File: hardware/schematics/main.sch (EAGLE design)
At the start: 332 parts, among them IC1 74LS257N, IC10 74S181N, IC100 74S257N, IC101 74LS377N, IC102 74LS377N, IC103 74S153N, IC104 74LS257N, IC105 74LS148N, IC106 74LS377N, IC107 74LS74N, IC108 74LS74N, IC109 74LS377N, IC11 74S181N, IC110 74LS377N, IC111 74LS253N, IC112 74LS257N, IC113 74LS253N, IC114 74LS257N, IC115 74LS04N, IC116 74S153N, IC117 74LS377N, IC118 74LS257N, IC119 74S08N, IC12 74LS151N, IC120 74LS244N, IC121 74LS257N, IC122 74LS257N, IC123 74LS377N, IC124 74S153N, IC125 74LS257N, IC126 74LS74N, IC127 74LS257N, IC128 74157N, IC129 74157N, IC13 74LS257N, IC130 74LS151N, IC131 74157N, IC132 74157N, IC133 74LS151N, IC134 74273N, IC135 74273N, IC136 74273N, IC137 74LS74N, IC138 74LS04N, IC139 74LS00N, IC14 74LS151N, IC141 74LS151N, IC142 74LS257N, IC143 74LS08N, IC144 74LS151N, IC145 7410N, IC146 74LS08N, IC147 74LS257N, IC148 74LS00N, IC149 74LS138N, IC15 74LS257N, IC150 74HC244N, IC151 7432N, IC152 74LS151N, IC153 7432N, IC154 74LS04N, IC155 74LS04N, IC156 74LS04N, IC157 74LS377N, IC158 74LS377N, IC159 74LS377N, IC16 74LS151N, IC160 74LS151N, IC161 74LS244N, IC162 74LS377N, IC163 74LS244N, IC164 74LS138N, IC165 74LS377N, IC166 74LS377N, IC167 7432N, IC168 74LS20N, IC169 74LS377N, IC17 74HC244N, IC170 74LS253N, IC171 74LS377N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

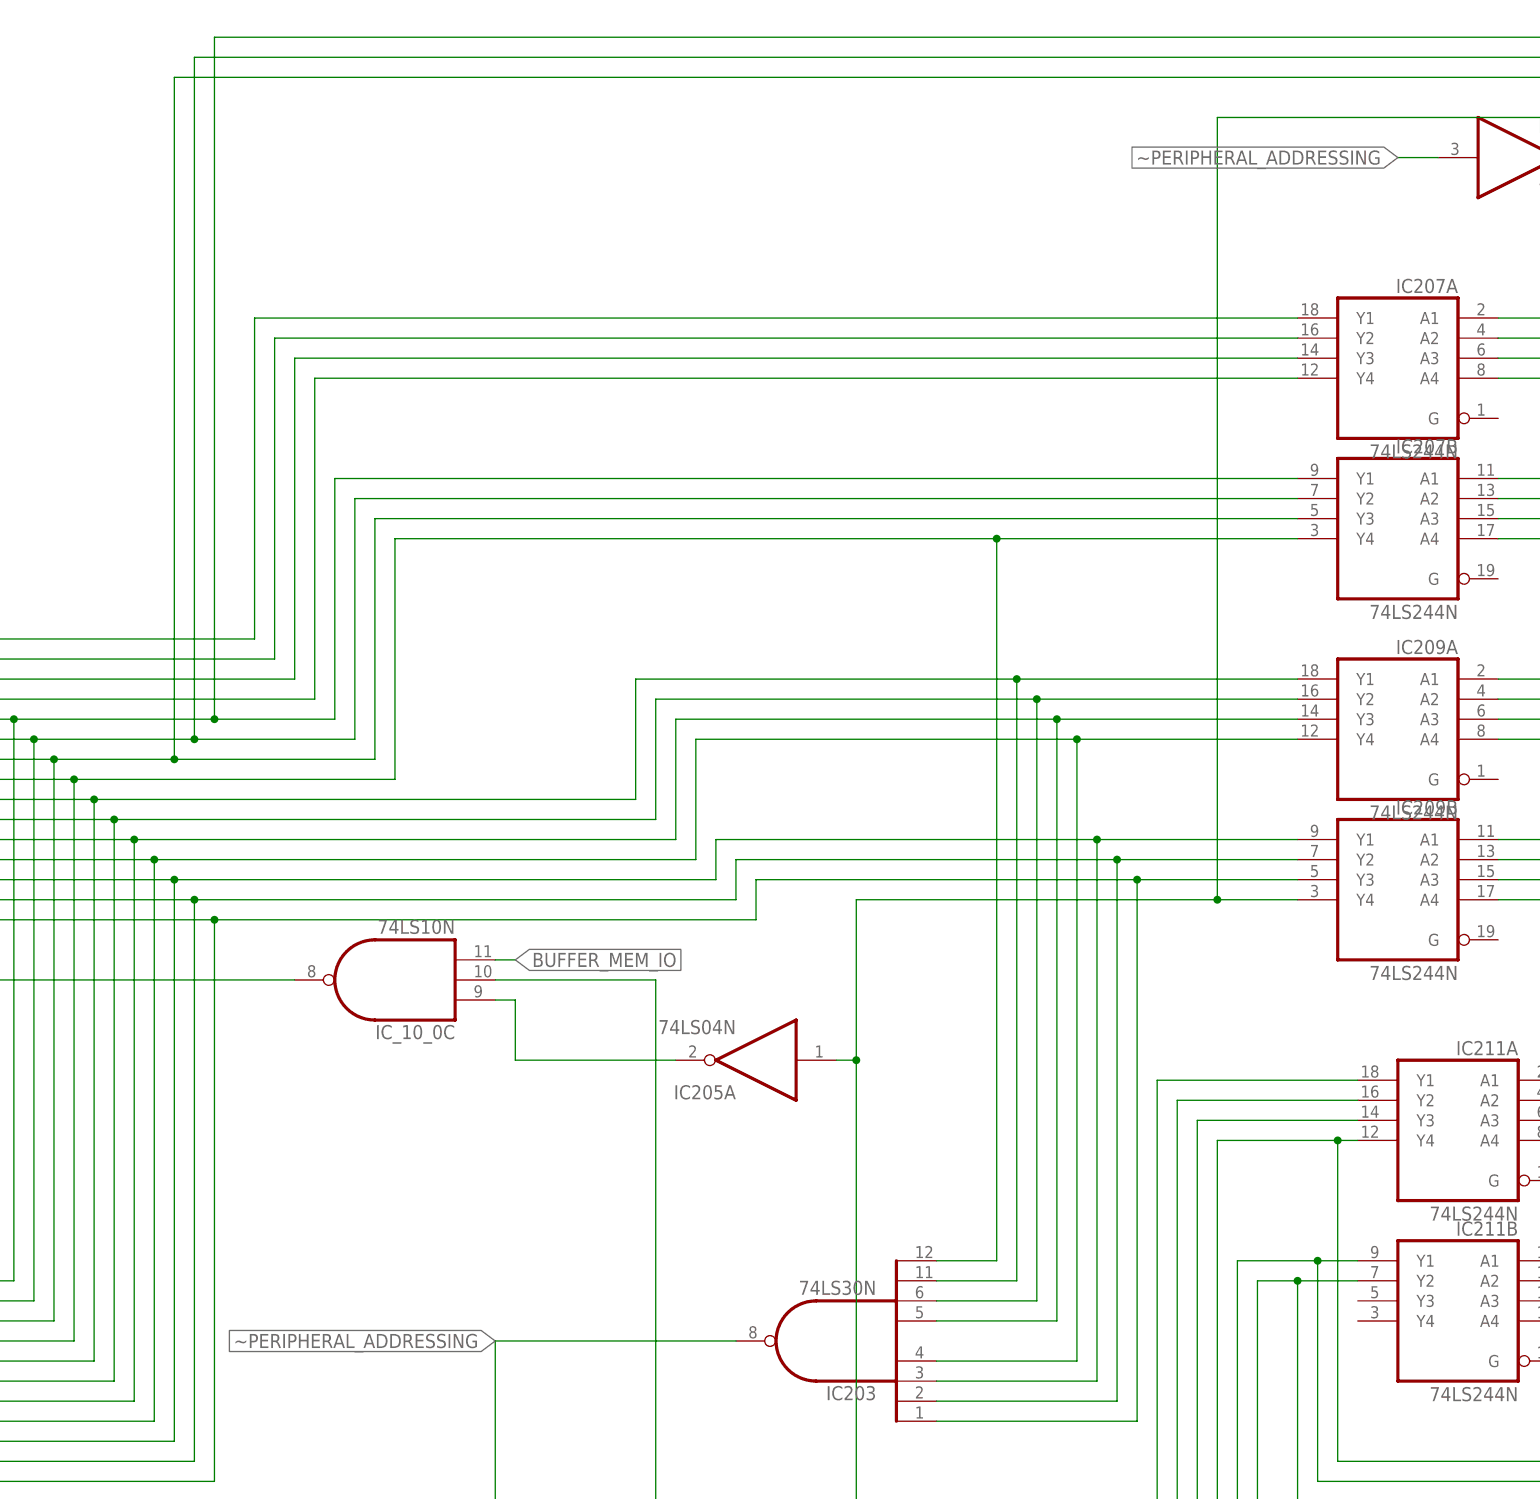
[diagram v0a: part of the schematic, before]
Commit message: added sol-1 web page
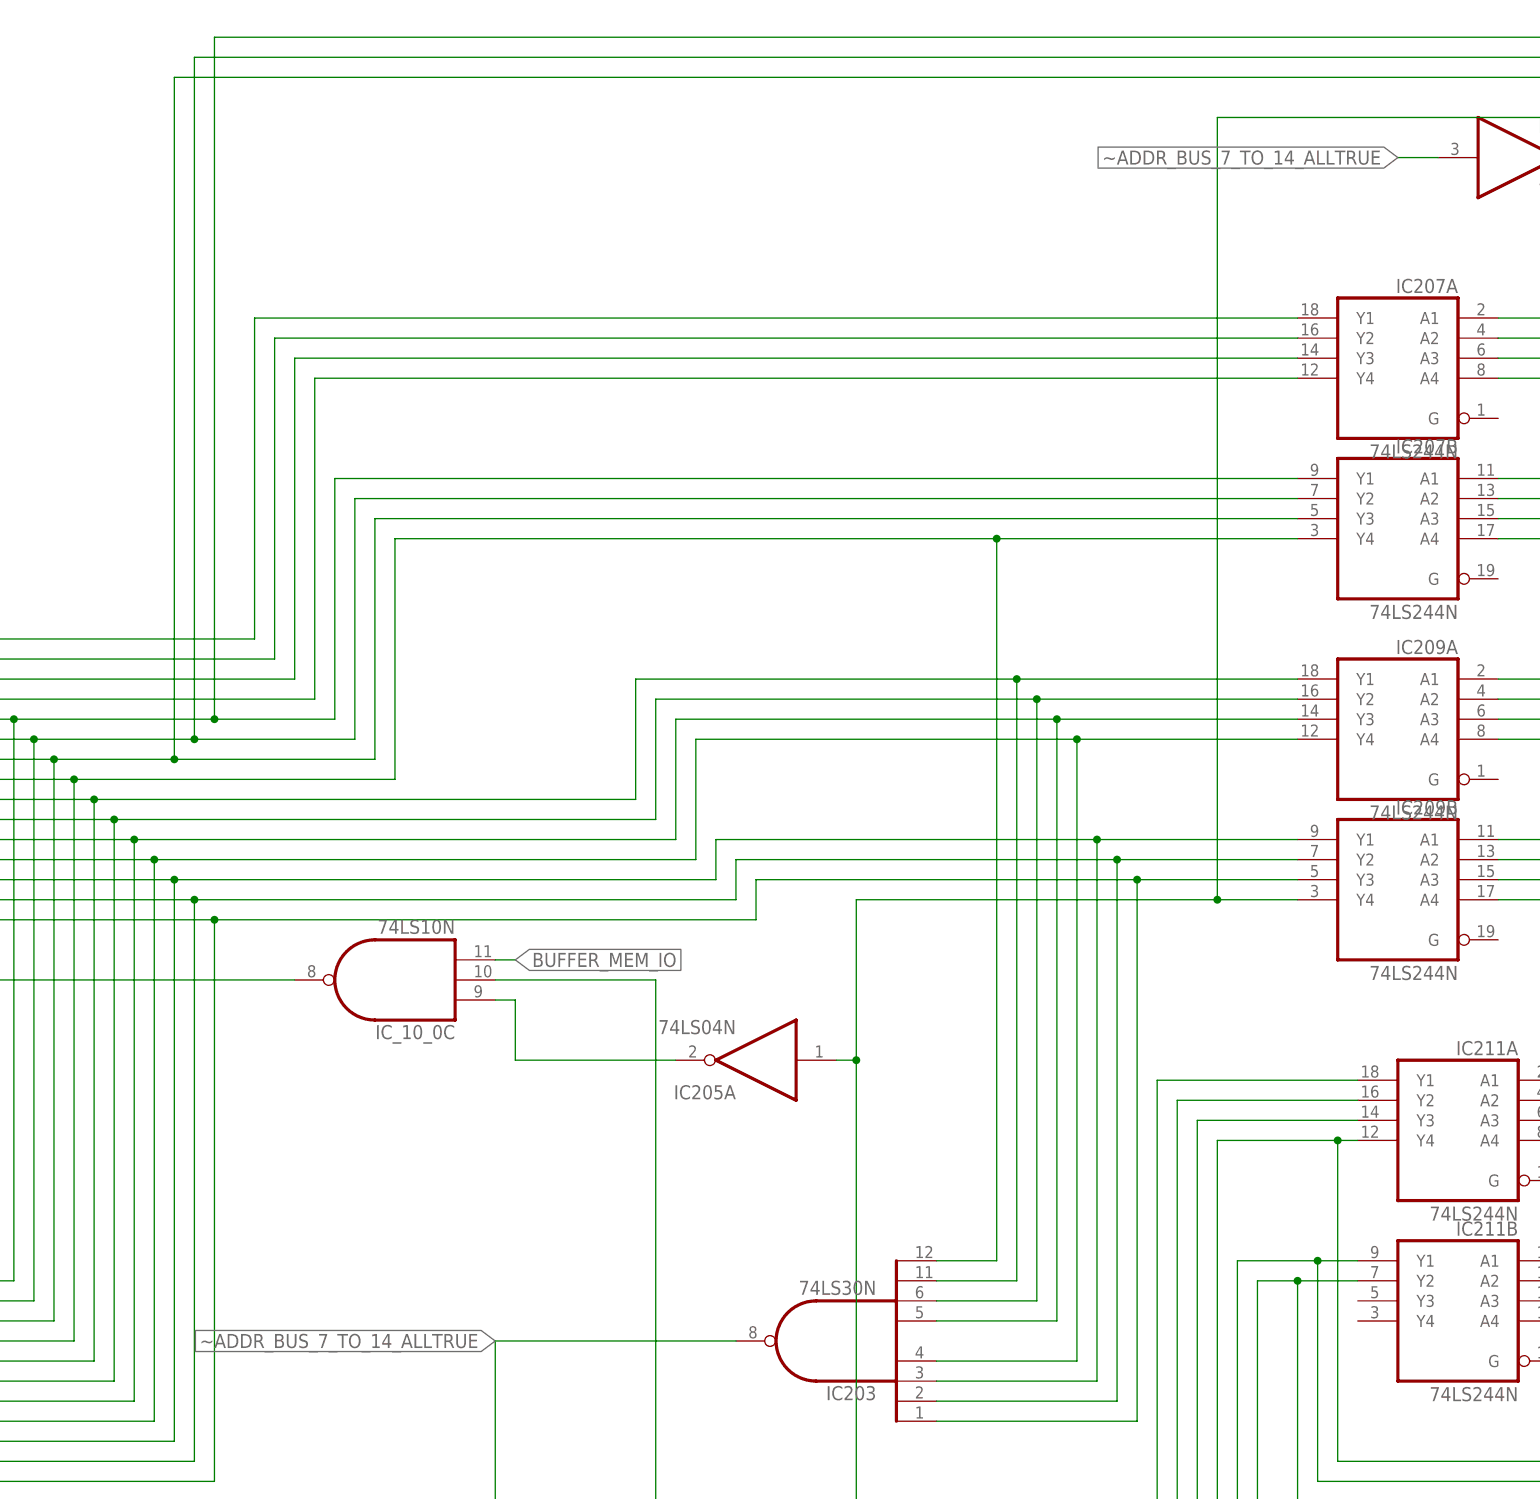
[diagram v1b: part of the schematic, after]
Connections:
- net ~PERIPHERAL_ADDRESSING renamed ~ADDR_BUS_7_TO_14_ALLTRUE
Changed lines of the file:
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@@
 </segment>
 </net>
-<net name="~PERIPHERAL_ADDRESSING" class="0">
+<net name="~ADDR_BUS_7_TO_14_ALLTRUE" class="0">
 <segment>
 <wire x1="228.6" y1="1209.04" x2="223.52" y2="1209.04" width="0.1524" layer="91"/>
